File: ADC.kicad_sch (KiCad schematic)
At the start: 92 parts, among them J1 Conn_01x03_Pin, J2 Screw_Terminal_01x02, J3 Screw_Terminal_01x09, SW1 SW_SPDT, U1 ADS1256IDBR, U10 CD4514BM, U12 ADR421ARMZ, U2 MCU-STM32F407VET6_LQFP100_, U3 ADM2483xRW, U4 LM2596S-5, U5 DCP010505BP, U6 MAX4052ESE, U7 OPA211ID, U8 AMS1117-3.3, U9 ADG5412FBCPZ-RL7, Y1 8MHz, Y2 ABM3B-25.000MHZ-D2Y-T

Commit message: thêm tiền sử lí ADC
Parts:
- removed U6: MAX4052ESE, MAX4052ESE:SOIC127P600X175-16N, symbol MAX4052ESE:MAX4052ESE
- added R1, R31, R37, R43, R55, R56, R57, R58: 2k, symbol Device:R
- added R25, R32, R38, R44, R59, R62, R65, R68: 1k, symbol Device:R
- added R26, R27, R33, R34, R39, R40, R45, R46, R60, R61, R63, R64, R66, R67, R69, R70: 500, symbol Device:R
- added R28, R30, R36, R42, R51, R52, R53, R54: 200, symbol Device:R
- added R29, R3, R35, R41, R47, R48, R49, R50: 190, symbol Device:R
- added U11, U14, U16, U20, U21, U22, U23: ADG5412FBCPZ-RL7, ADG5412FBCPZ-RL7:QFN65P400X400X80-17N, symbol ADG5412FBCPZ-RL7:ADG5412FBCPZ-RL7
- added U13, U15, U17, U24, U25, U26, U27: OPA211ID, OPA211ID:SOIC127P599X175-8N, symbol OPA211ID:OPA211ID
- added U19: CD4514BM, CD4514BM:SOIC127P1030X265-24N, symbol CD4514BM:CD4514BM
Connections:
- net +12V: now also U7.7 (V+), U9.11 (VDD), U11.11 (VDD), U13.7 (V+), U14.11 (VDD), U15.7 (V+), U16.11 (VDD), U17.7 (V+), U20.11 (VDD), U21.11 (VDD), U22.11 (VDD), U23.11 (VDD), U24.7 (V+), U25.7 (V+), U26.7 (V+), U27.7 (V+)
- net -12V: now also U7.4 (V-), U9.2 (VSS), U11.2 (VSS), U13.4 (V-), U14.2 (VSS), U15.4 (V-), U16.2 (VSS), U17.4 (V-), U20.2 (VSS), U21.2 (VSS), U22.2 (VSS), U23.2 (VSS), U24.4 (V-), U25.4 (V-), U26.4 (V-), U27.4 (V-)
- net GND: now also U9.3 (GND), U9.4 (S4), R27.1, R34.1, R40.1, R46.1, R61.1, R64.1, R67.1, R70.1, U11.3 (GND), U11.4 (S4), U14.3 (GND), U14.4 (S4), U16.3 (GND), U16.4 (S4), U20.3 (GND), U20.4 (S4), U21.3 (GND), U21.4 (S4), U22.3 (GND), U22.4 (S4), U23.3 (GND), U23.4 (S4)
- net VinN1: no longer R5.2
- net VinN2: no longer R7.2
- net VinN3: no longer R9.2
- net VinN4: no longer R12.2
- net VinP1: now also U7.3 (+IN), U13.3 (+IN), U15.3 (+IN), U17.3 (+IN), U24.3 (+IN), U25.3 (+IN), U26.3 (+IN), U27.3 (+IN); no longer R4.2
- net VinP2: no longer R6.2
- net VinP3: no longer R8.2
- net VinP4: no longer R10.2
- net DECODER1_6: now reaches U10.1 (STROBE)
- net DECODER1_6: now also U2.34 (PC5)
- net at U10.10 (S1): now also U9.14 (IN2)
- net at U10.11 (S0): now also U9.15 (IN1)
- net at U10.13 (S13): now also U16.14 (IN2)
- net at U10.14 (S12): now also U16.15 (IN1)
- net at U10.15 (S15): now also U16.6 (IN4)
- net at U10.16 (S14): now also U16.7 (IN3)
- net at U10.17 (S9): now also U14.14 (IN2)
- net at U10.18 (S8): now also U14.15 (IN1)
- net at U10.19 (S11): now also U14.6 (IN4)
- net DECODER1_1: now reaches U10.2 (DATA1)
- net DECODER1_1: now also U2.15 (PC0)
- net at U10.20 (S10): now also U14.7 (IN3)
- net DECODER1_3: now reaches U10.21 (DATA3)
- net DECODER1_3: now also U2.17 (PC2)
- net DECODER1_4: now reaches U10.22 (DATA4)
- net DECODER1_4: now also U2.18 (PC3)
- net DECODER1_5: now reaches U10.23 (INHIBIT)
- net DECODER1_5: now also U2.33 (PC4)
- net DECODER1_2: now reaches U10.3 (DATA2)
- net DECODER1_2: now also U2.16 (PC1)
- net at U10.4 (S7): now also U11.6 (IN4)
- net at U10.5 (S6): now also U11.7 (IN3)
- net at U10.6 (S5): now also U11.14 (IN2)
- net at U10.7 (S4): now also U11.15 (IN1)
- net at U10.8 (S3): now also U9.6 (IN4)
- net at U10.9 (S2): now also U9.7 (IN3)
- net at U7.2 (-IN): now also R1.1, R3.1
- net at U7.6 (OUT): now also R1.2, R25.2, R28.1
- net ADC1: now reaches U9.1 (S1)
- net ADC1: now also R4.2, U9.12 (S2), U9.9 (S3), U11.1 (S1), U11.12 (S2), U11.9 (S3), U14.1 (S1), U14.12 (S2), U14.9 (S3), U16.1 (S1), U16.12 (S2), U16.9 (S3), U20.1 (S1), U20.12 (S2), U20.9 (S3), U21.1 (S1), U21.12 (S2), U21.9 (S3), U22.1 (S1), U22.12 (S2), U22.9 (S3), U23.1 (S1), U23.12 (S2), U23.9 (S3)
- net at U9.13 (D2): now also R25.1, R26.2
- net at U9.16 (D1): now also R26.1, R27.2
- net at U9.5 (D4): now also R3.2
- net at U9.8 (D3): now also R28.2
- net DECODER2_1: now reaches U2.63 (PC6)
- net DECODER2_1: now also U19.2 (DATA1)
- net DECODER2_2: now reaches U2.64 (PC7)
- net DECODER2_2: now also U19.3 (DATA2)
- net DECODER2_3: now reaches U2.65 (PC8)
- net DECODER2_3: now also U19.21 (DATA3)
- net DECODER2_4: now reaches U2.66 (PC9)
- net DECODER2_4: now also U19.22 (DATA4)
- net DECODER2_5: now reaches U2.78 (PC10)
- net DECODER2_5: now also U19.23 (INHIBIT)
- net DECODER2_6: now reaches U2.79 (PC11)
- net DECODER2_6: now also U19.1 (STROBE)
- new net: R36.1, R37.2, R38.2, U15.6 (OUT)
- new net: R36.2, U14.8 (D3)
- new net: R63.1, R64.2, U21.16 (D1)
- new net: R44.1, R45.2, U16.13 (D2)
- new net: R42.1, R43.2, R44.2, U17.6 (OUT)
- new net: R62.1, R63.2, U21.13 (D2)
- new net: R30.1, R31.2, R32.2, U13.6 (OUT)
- new net: R30.2, U11.8 (D3)
- new net: R53.1, R57.2, R65.2, U26.6 (OUT)
- new net: R53.2, U22.8 (D3)
- new net: R33.1, R34.2, U11.16 (D1)
- new net: R32.1, R33.2, U11.13 (D2)
- new net: R45.1, R46.2, U16.16 (D1)
- new net: R49.1, R57.1, U26.2 (-IN)
- new net: R49.2, U22.5 (D4)
- new net: R68.1, R69.2, U23.13 (D2)
- new net: U19.6 (S5), U23.14 (IN2)
- new net: U19.7 (S4), U23.15 (IN1)
- new net: R69.1, R70.2, U23.16 (D1)
- new net: R50.2, U23.5 (D4)
- new net: U19.4 (S7), U23.6 (IN4)
- new net: U19.5 (S6), U23.7 (IN3)
- new net: R54.2, U23.8 (D3)
- new net: R52.1, R56.2, R62.2, U25.6 (OUT)
- new net: R42.2, U16.8 (D3)
- new net: R52.2, U21.8 (D3)
- new net: R47.1, R55.1, U24.2 (-IN)
- new net: R51.1, R55.2, R59.2, U24.6 (OUT)
- new net: R29.1, R31.1, U13.2 (-IN)
- new net: R29.2, U11.5 (D4)
- new net: R35.1, R37.1, U15.2 (-IN)
- new net: R38.1, R39.2, U14.13 (D2)
- new net: R39.1, R40.2, U14.16 (D1)
- new net: R35.2, U14.5 (D4)
- new net: U19.10 (S1), U22.14 (IN2)
- new net: U19.11 (S0), U22.15 (IN1)
- new net: U19.13 (S13), U21.14 (IN2)
- new net: U19.14 (S12), U21.15 (IN1)
- new net: U19.15 (S15), U21.6 (IN4)
- new net: U19.16 (S14), U21.7 (IN3)
- new net: U19.17 (S9), U20.14 (IN2)
- new net: U19.18 (S8), U20.15 (IN1)
- new net: U19.19 (S11), U20.6 (IN4)
- new net: U19.20 (S10), U20.7 (IN3)
- new net: U19.8 (S3), U22.6 (IN4)
- new net: U19.9 (S2), U22.7 (IN3)
- new net: R50.1, R58.1, U27.2 (-IN)
- new net: R54.1, R58.2, R68.2, U27.6 (OUT)
- new net: R41.1, R43.1, U17.2 (-IN)
- new net: R60.1, R61.2, U20.16 (D1)
- new net: R47.2, U20.5 (D4)
- new net: R48.1, R56.1, U25.2 (-IN)
- new net: R59.1, R60.2, U20.13 (D2)
- new net: R48.2, U21.5 (D4)
- new net: R65.1, R66.2, U22.13 (D2)
- new net: R66.1, R67.2, U22.16 (D1)
- new net: R41.2, U16.5 (D4)
- new net: R51.2, U20.8 (D3)
- new net ADC2: R5.2
- new net ADC3: R6.2
- new net ADC4: R7.2
- new net ADC5: R8.2
- new net ADC6: R9.2
- new net ADC7: R10.2
- new net ADC8: R12.2
- no-connect marks 82 -> 70
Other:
- moved on the sheet: C1, C12, C13, C14, C15, C16, C17, C18, C19, C2, C20, C21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

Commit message: update
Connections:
- net +3.3V: now also U10.24 (VDD), U19.24 (VDD)
- net GND: now also U10.12 (VSS), U19.12 (VSS)

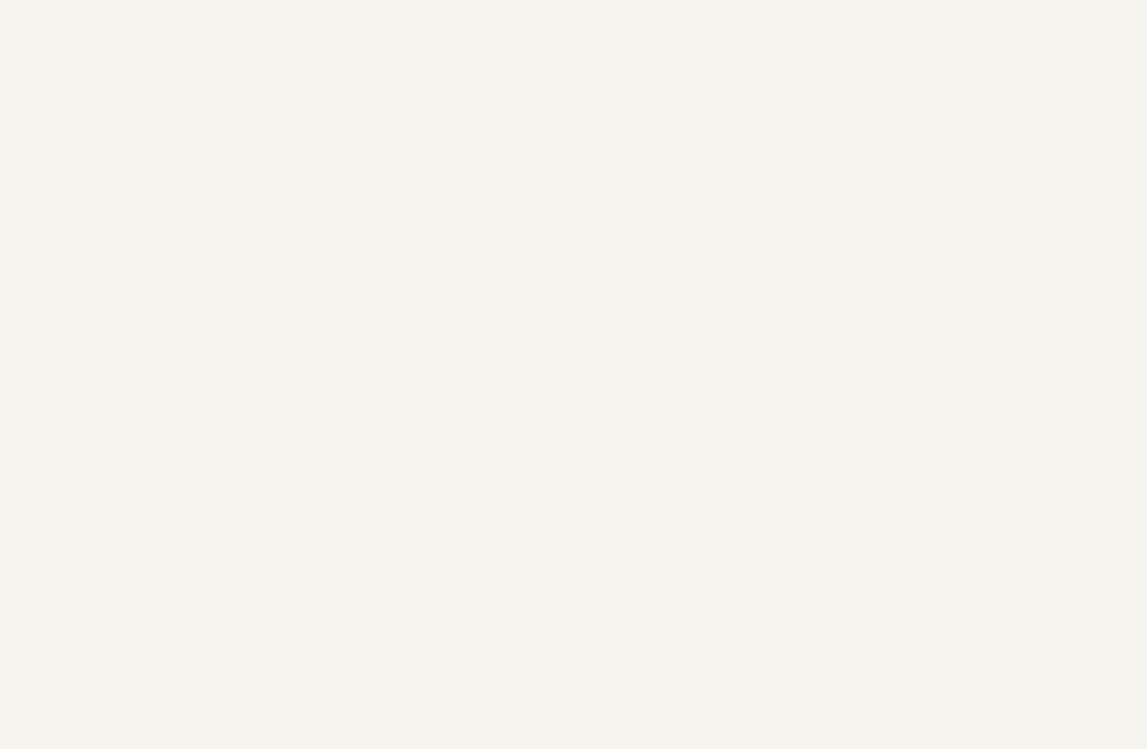
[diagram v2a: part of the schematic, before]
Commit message: Add linh kiên
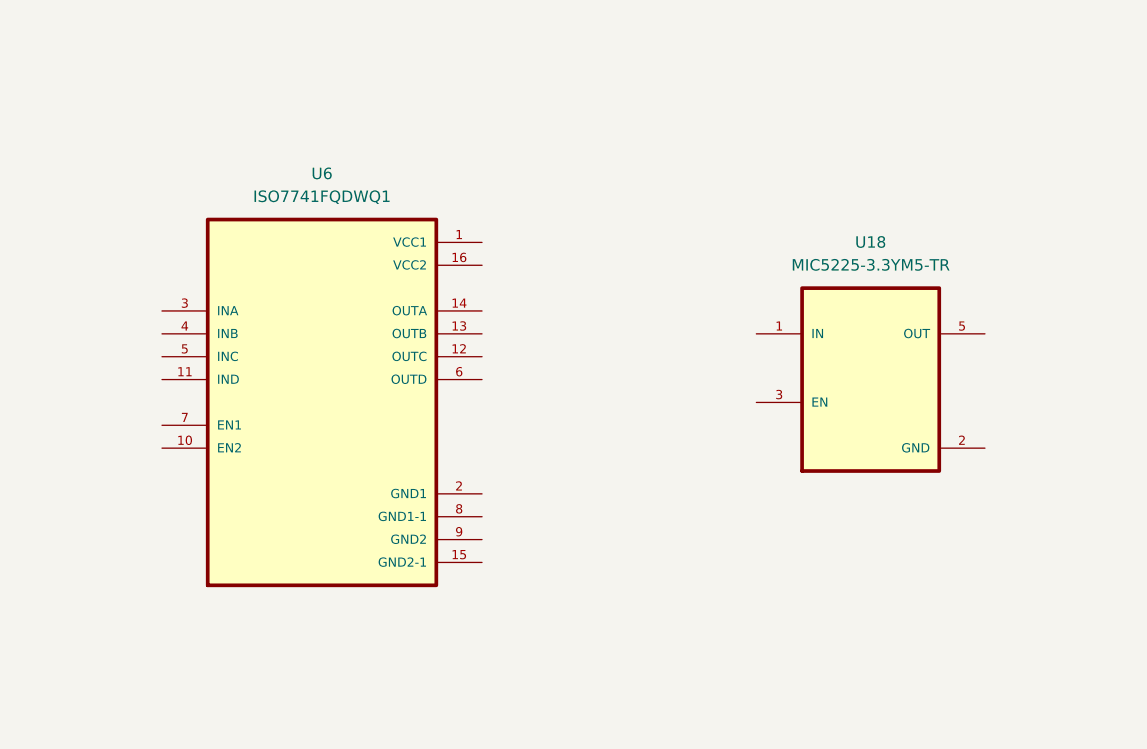
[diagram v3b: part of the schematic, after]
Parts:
- added U18: MIC5225-3.3YM5-TR, MIC5225-3.3YM5-TR:SOT95P280X145-5N, symbol MIC5225-3.3YM5-TR:MIC5225-3.3YM5-TR
- added U6: ISO7741FQDWQ1, ISO7741FQDWQ1:SOIC127P1030X265-16N, symbol ISO7741FQDWQ1:ISO7741FQDWQ1

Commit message: ok roài
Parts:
- removed U18: MIC5225-3.3YM5-TR, MIC5225-3.3YM5-TR:SOT95P280X145-5N, symbol MIC5225-3.3YM5-TR:MIC5225-3.3YM5-TR
- removed U6: ISO7741FQDWQ1, ISO7741FQDWQ1:SOIC127P1030X265-16N, symbol ISO7741FQDWQ1:ISO7741FQDWQ1
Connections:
- net ADC1: no longer U11.1 (S1), U11.12 (S2), U11.9 (S3), U14.1 (S1), U14.12 (S2), U14.9 (S3), U16.1 (S1), U16.12 (S2), U16.9 (S3), U20.1 (S1), U20.12 (S2), U20.9 (S3), U21.1 (S1), U21.12 (S2), U21.9 (S3), U22.1 (S1), U22.12 (S2), U22.9 (S3), U23.1 (S1), U23.12 (S2), U23.9 (S3)
- net ADC2: now also U11.1 (S1), U11.12 (S2), U11.9 (S3)
- net ADC3: now also U14.1 (S1), U14.12 (S2), U14.9 (S3)
- net ADC4: now also U16.1 (S1), U16.12 (S2), U16.9 (S3)
- net ADC5: now also U22.1 (S1), U22.12 (S2), U22.9 (S3)
- net ADC6: now also U23.1 (S1), U23.12 (S2), U23.9 (S3)
- net ADC7: now also U20.1 (S1), U20.12 (S2), U20.9 (S3)
- net ADC8: now also U21.1 (S1), U21.12 (S2), U21.9 (S3)
- net GND: now also U11.17 (EP), U14.17 (EP), U16.17 (EP), U20.17 (EP), U21.17 (EP), U22.17 (EP), U23.17 (EP), U9.17 (EP)
- net VinP1: no longer U13.3 (+IN), U15.3 (+IN), U17.3 (+IN), U24.3 (+IN), U25.3 (+IN), U26.3 (+IN), U27.3 (+IN)
- net VinP2: now also U13.3 (+IN)
- net VinP3: now also U15.3 (+IN)
- net VinP4: now also U17.3 (+IN)
- new net VinP5: U26.3 (+IN)
- new net VinP6: U27.3 (+IN)
- new net VinP7: U24.3 (+IN)
- new net VinP8: U25.3 (+IN)
- no-connect marks 70 -> 78
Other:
- moved on the sheet: C12, C13, C14, C15, C16, C17, C18, C19, C20, C21, C22, C23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

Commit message: aaa
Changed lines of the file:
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@@
 	)
 	(junction
+		(at 393.7 81.28)
+		(diameter 0)
+		(color 0 0 0 0)
+	)
+	(junction
 		(at 990.6 500.38)
 		(diameter 0)
@@
 	)
 	(junction
-		(at 360.68 81.28)
-		(diameter 0)
-		(color 0 0 0 0)
-	)
-	(junction
 		(at 755.65 267.97)
 		(diameter 0)
@@
 	(wire
 		(pts
+			(xy 393.7 81.28) (xy 400.05 81.28)
+		)
+		(stroke
+			(width 0)
+			(type default)
+		)
+	)
+	(wire
+		(pts
 			(xy 927.1 345.44) (xy 927.1 346.71)
 		)
@@
 	(wire
 		(pts
-			(xy 355.6 81.28) (xy 360.68 81.28)
+			(xy 355.6 81.28) (xy 372.11 81.28)
 		)
 		(stroke
@@
 	(wire
 		(pts
-			(xy 360.68 81.28) (xy 372.11 81.28)
-		)
-		(stroke
-			(width 0)
-			(type default)
-		)
-	)
-	(wire
-		(pts
 			(xy 383.54 81.28) (xy 383.54 86.36)
 		)
@@
 	(wire
 		(pts
-			(xy 391.16 81.28) (xy 400.05 81.28)
+			(xy 391.16 81.28) (xy 393.7 81.28)
 		)
 		(stroke
@@
 	)
 	(symbol
-		(lib_id "power:PWR_FLAG")
-		(at 360.68 81.28 0)
-		(unit 1)
-		(exclude_from_sim no)
-		(in_bom yes)
-		(on_board yes)
-		(dnp no)
-		(fields_autoplaced yes)
-		(property "Reference" "#FLG02"
-			(at 360.68 79.375 0)
-			(effects
-				(font
-					(size 1.27 1.27)
-				)
-				(hide yes)
-			)
-		)
-		(property "Value" "PWR_FLAG"
-			(at 360.68 76.2 0)
-			(effects
-				(font
-					(size 1.27 1.27)
-				)
-			)
-		)
-		(property "Footprint" ""
-			(at 360.68 81.28 0)
-			(effects
-				(font
-					(size 1.27 1.27)
-				)
-				(hide yes)
-			)
-		)
-		(property "Datasheet" "~"
-			(at 360.68 81.28 0)
-			(effects
-				(font
-					(size 1.27 1.27)
-				)
-				(hide yes)
-			)
-		)
-		(property "Description" "Special symbol for telling ERC where power comes from"
-			(at 360.68 81.28 0)
-			(effects
-				(font
-					(size 1.27 1.27)
-				)
-				(hide yes)
-			)
-		)
-		(pin "1"
-		)
-		(instances
-			(project "ADC"
-				(path "/c7ceee6a-ba62-44b0-b5ba-f64f163625fc"
-					(reference "#FLG02")
-					(unit 1)
-				)
-			)
-		)
-	)
-	(symbol
 		(lib_id "power:+5V")
 		(at 607.06 398.78 0)
@@
 					(unit 1)
 				)
+			)
+		)
+	)
+	(symbol
+		(lib_id "power:PWR_FLAG")
+		(at 393.7 81.28 0)
+		(unit 1)
+		(exclude_from_sim no)
+		(in_bom yes)
+		(on_board yes)
+		(dnp no)
+		(fields_autoplaced yes)
+		(property "Reference" "#FLG02"
+			(at 393.7 79.375 0)
+			(effects
+				(font
+					(size 1.27 1.27)
+				)
+				(hide yes)
+			)
+		)
+		(property "Value" "PWR_FLAG"
+			(at 393.7 76.2 0)
+			(effects
+				(font
+					(size 1.27 1.27)
+				)
+			)
+		)
+		(property "Footprint" ""
+			(at 393.7 81.28 0)
+			(effects
+				(font
+					(size 1.27 1.27)
+				)
+				(hide yes)
+			)
+		)
+		(property "Datasheet" "~"
+			(at 393.7 81.28 0)
+			(effects
+				(font
+					(size 1.27 1.27)
+				)
+				(hide yes)
+			)
+		)
+		(property "Description" "Special symbol for telling ERC where power comes from"
+			(at 393.7 81.28 0)
+			(effects
+				(font
+					(size 1.27 1.27)
+				)
+				(hide yes)
+			)
+		)
+		(pin "1"
+		)
+		(instances
+			(project "ADC"
+				(path "/c7ceee6a-ba62-44b0-b5ba-f64f163625fc"
+					(reference "#FLG02")
+					(unit 1)
+				)

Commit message: Them bao ve
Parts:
- added D10, D11, D12, D13, D14, D7, D8, D9: D_TVS_Filled, symbol Device:D_TVS_Filled
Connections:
- net GND: now also D10.1 (A1), D11.1 (A1), D12.1 (A1), D13.1 (A1), D14.1 (A1), D7.1 (A1), D8.1 (A1), D9.1 (A1)
- net VinN1: now also D8.2 (A2)
- net VinN2: now also D10.2 (A2)
- net VinN3: now also D12.2 (A2)
- net VinN4: now also D14.2 (A2)
- net VinP1: now also D7.2 (A2)
- net VinP2: now also D9.2 (A2)
- net VinP3: now also D11.2 (A2)
- net VinP4: now also D13.2 (A2)
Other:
- note added: "Isolated DC/DC converter"
- note added: "Power Supply 5v and +-12V"
- note removed: "Isolated DC/DC converters"
- note removed: "Power Supply 5v"

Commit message: Add TLV
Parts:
- added U6: TLV1704AIPWR, TLV1704AIPWR:SOP65P640X120-14N, symbol TLV1704AIPWR:TLV1704AIPWR
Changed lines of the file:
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@@
+	)
+	(symbol
+		(lib_id "TLV1704AIPWR:TLV1704AIPWR")
+		(at 110.49 605.79 0)
+		(unit 1)
+		(exclude_from_sim no)
+		(in_bom yes)
+		(on_board yes)
+		(dnp no)
+		(fields_autoplaced yes)
+		(property "Reference" "U6"
+			(at 110.49 570.23 0)
+			(effects
+				(font
+					(size 1.27 1.27)
+				)
+			)
+		)
+		(property "Value" "TLV1704AIPWR"
+			(at 110.49 572.77 0)
+			(effects
+				(font
+					(size 1.27 1.27)
+				)
+			)
+		)
+		(property "Footprint" "TLV1704AIPWR:SOP65P640X120-14N"
+			(at 110.49 605.79 0)
+			(effects
+				(font
+					(size 1.27 1.27)
+				)
+				(justify bottom)
+				(hide yes)
+			)
+		)
+		(property "Datasheet" ""
+			(at 110.49 605.79 0)
+			(effects
+				(font
+					(size 1.27 1.27)
+				)
+				(hide yes)
+			)
+		)
+		(property "Description" ""
+			(at 110.49 605.79 0)
+			(effects
+				(font
+					(size 1.27 1.27)
+				)
+				(hide yes)
+			)
+		)
+		(property "MF" "Texas Instruments"
+			(at 110.49 605.79 0)
+			(effects
+				(font
+					(size 1.27 1.27)
+				)
+				(justify bottom)
+				(hide yes)
+			)
+		)
+		(property "Description_1" "\n                        \n                            Quad high voltage, low power comparator\n                        \n"
+			(at 110.49 605.79 0)
+			(effects
+				(font
+					(size 1.27 1.27)
+				)
+				(justify bottom)
+				(hide yes)
+			)
+		)
+		(property "Package" "TSSOP-14 Texas Instruments"
+			(at 110.49 605.79 0)
+			(effects
+				(font
+					(size 1.27 1.27)
+				)
+				(justify bottom)
+				(hide yes)
+			)
+		)
+		(property "Price" "None"
+			(at 110.49 605.79 0)
+			(effects
+				(font
+					(size 1.27 1.27)
+				)
+				(justify bottom)
+				(hide yes)
+			)
+		)
+		(property "SnapEDA_Link" "https://www.snapeda.com/parts/TLV1704AIPWR/Texas+Instruments/view-part/?ref=snap"
+			(at 110.49 605.79 0)
+			(effects
+				(font
+					(size 1.27 1.27)
+				)
+				(justify bottom)
+				(hide yes)
+			)
+		)
+		(property "MP" "TLV1704AIPWR"
+			(at 110.49 605.79 0)
+			(effects
+				(font
+					(size 1.27 1.27)
+				)
+				(justify bottom)
+				(hide yes)
+			)
+		)
+		(property "Availability" "In Stock"
+			(at 110.49 605.79 0)
+			(effects
+				(font
+					(size 1.27 1.27)
+				)
+				(justify bottom)
+				(hide yes)
+			)
+		)
+		(property "Check_prices" "https://www.snapeda.com/parts/TLV1704AIPWR/Texas+Instruments/view-part/?ref=eda"
+			(at 110.49 605.79 0)
+			(effects
+				(font
+					(size 1.27 1.27)
+				)
+				(justify bottom)
+				(hide yes)
+			)
+		)
+		(pin "5"
+		)
+		(pin "6"
+		)
+		(pin "13"
+		)
+		(pin "14"
+		)
+		(pin "12"
+		)
+		(pin "2"
+		)
+		(pin "3"
+		)
+		(pin "4"
+		)
+		(pin "1"
+		)
+		(pin "9"
+		)
+		(pin "8"
+		)
+		(pin "7"
+		)
+		(pin "11"
+		)
+		(pin "10"
+		)
+		(instances
+			(project ""
+				(path "/c7ceee6a-ba62-44b0-b5ba-f64f163625fc"
+					(reference "U6")
+					(unit 1)
+				)
+			)
+		)
 	)
 	(symbol

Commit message: add CD
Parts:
- added U18: CD4072BM, CD4072BM:SOIC127P600X175-14N, symbol CD4072BM:CD4072BM
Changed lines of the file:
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@@
+	)
+	(symbol
+		(lib_id "CD4072BM:CD4072BM")
+		(at 111.76 482.6 0)
+		(unit 1)
+		(exclude_from_sim no)
+		(in_bom yes)
+		(on_board yes)
+		(dnp no)
+		(fields_autoplaced yes)
+		(property "Reference" "U18"
+			(at 111.76 459.74 0)
+			(effects
+				(font
+					(size 1.27 1.27)
+				)
+			)
+		)
+		(property "Value" "CD4072BM"
+			(at 111.76 462.28 0)
+			(effects
+				(font
+					(size 1.27 1.27)
+				)
+			)
+		)
+		(property "Footprint" "CD4072BM:SOIC127P600X175-14N"
+			(at 111.76 482.6 0)
+			(effects
+				(font
+					(size 1.27 1.27)
+				)
+				(justify bottom)
+				(hide yes)
+			)
+		)
+		(property "Datasheet" ""
+			(at 111.76 482.6 0)
+			(effects
+				(font
+					(size 1.27 1.27)
+				)
+				(hide yes)
+			)
+		)
+		(property "Description" ""
+			(at 111.76 482.6 0)
+			(effects
+				(font
+					(size 1.27 1.27)
+				)
+				(hide yes)
+			)
+		)
+		(property "MF" "Texas Instruments"
+			(at 111.76 482.6 0)
+			(effects
+				(font
+					(size 1.27 1.27)
+				)
+				(justify bottom)
+				(hide yes)
+			)
+		)
+		(property "Description_1" "\n                        \n                            2-ch, 4-input, 3-V to 18-V OR gates\n                        \n"
+			(at 111.76 482.6 0)
+			(effects
+				(font
+					(size 1.27 1.27)
+				)
+				(justify bottom)
+				(hide yes)
+			)
+		)
+		(property "Package" "SOIC-14 Texas Instruments"
+			(at 111.76 482.6 0)
+			(effects
+				(font
+					(size 1.27 1.27)
+				)
+				(justify bottom)
+				(hide yes)
+			)
+		)
+		(property "Price" "None"
+			(at 111.76 482.6 0)
+			(effects
+				(font
+					(size 1.27 1.27)
+				)
+				(justify bottom)
+				(hide yes)
+			)
+		)
+		(property "SnapEDA_Link" "https://www.snapeda.com/parts/CD4072BM/Texas+Instruments/view-part/?ref=snap"
+			(at 111.76 482.6 0)
+			(effects
+				(font
+					(size 1.27 1.27)
+				)
+				(justify bottom)
+				(hide yes)
+			)
+		)
+		(property "MP" "CD4072BM"
+			(at 111.76 482.6 0)
+			(effects
+				(font
+					(size 1.27 1.27)
+				)
+				(justify bottom)
+				(hide yes)
+			)
+		)
+		(property "Availability" "In Stock"
+			(at 111.76 482.6 0)
+			(effects
+				(font
+					(size 1.27 1.27)
+				)
+				(justify bottom)
+				(hide yes)
+			)
+		)
+		(property "Check_prices" "https://www.snapeda.com/parts/CD4072BM/Texas+Instruments/view-part/?ref=eda"
+			(at 111.76 482.6 0)
+			(effects
+				(font
+					(size 1.27 1.27)
+				)
+				(justify bottom)
+				(hide yes)
+			)
+		)
+		(pin "3"
+		)
+		(pin "1"
+		)
+		(pin "10"
+		)
+		(pin "13"
+		)
+		(pin "2"
+		)
+		(pin "12"
+		)
+		(pin "4"
+		)
+		(pin "5"
+		)
+		(pin "14"
+		)
+		(pin "9"
+		)
+		(pin "11"
+		)
+		(pin "7"
+		)
+		(instances
+			(project ""
+				(path "/c7ceee6a-ba62-44b0-b5ba-f64f163625fc"
+					(reference "U18")
+					(unit 1)
+				)
+			)
+		)
 	)
 	(symbol
